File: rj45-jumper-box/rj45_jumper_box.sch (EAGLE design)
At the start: 4 parts, among them X1 SS-7188S-A-NF, X2 SS-7188S-A-NF

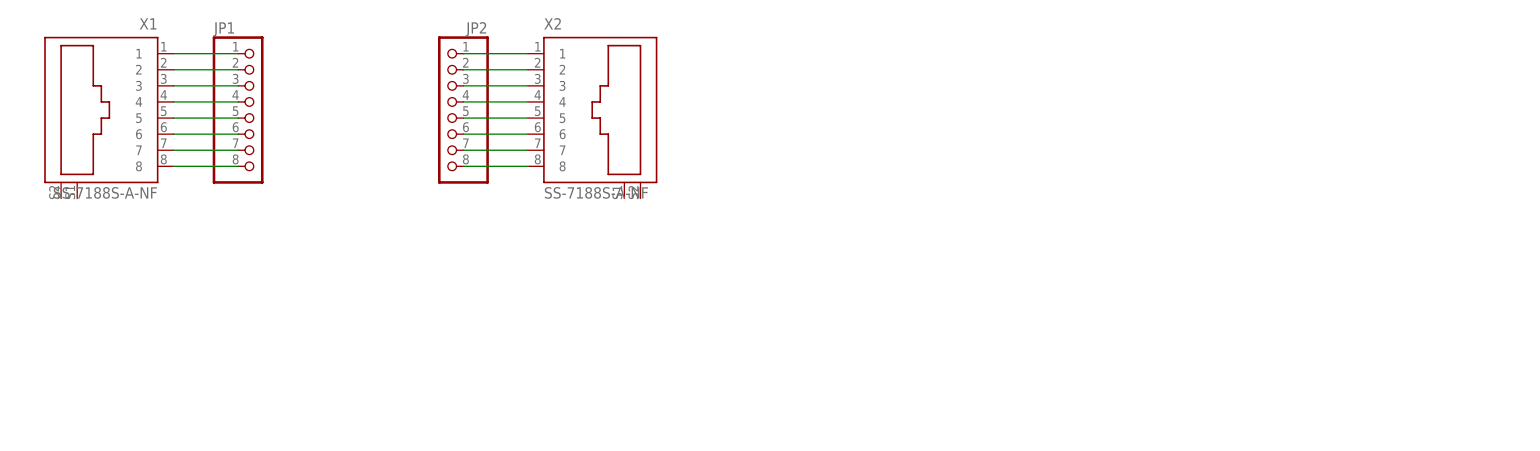
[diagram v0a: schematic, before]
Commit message: rj45_jumper_box: Use different RJ45 jack; both on top layer
The original design (one RJ45 on top, one on bottom) was easy to route
but was difficult to handle. Let's swap both connectors to top, and use
a low-cost Chinese RJ45.
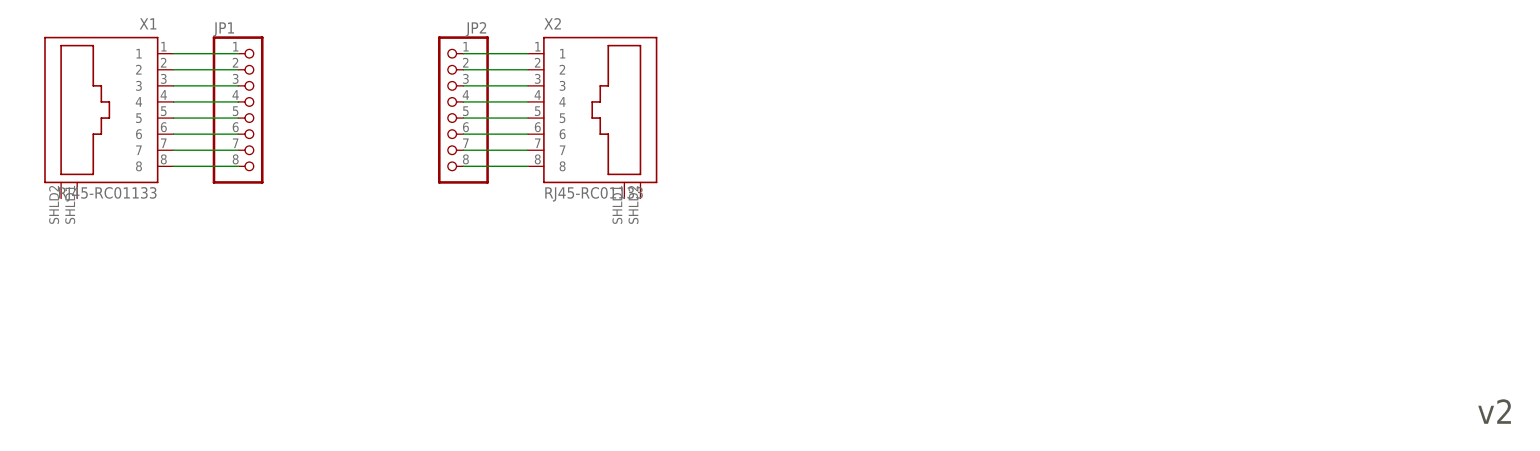
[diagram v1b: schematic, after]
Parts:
- X1, X2: value SS-7188S-A-NF -> RJ45-RC01133; device stewart-rj45:SS-7188S-A-NF -> stewart-rj45:RJ45-RC01133
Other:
- moved on the sheet: X1, X2
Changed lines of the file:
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@@
 <schematic xreflabel="%F%N/%S.%C%R" xrefpart="/%S.%C%R">
 <attributes>
+<attribute name="REVISION" value="v2"/>
 </attributes>
 <variantdefs>
@@
 </classes>
 <parts>
-<part name="X1" library="stewart-rj45" deviceset="SS-7188S-A-NF" device=""/>
-<part name="X2" library="stewart-rj45" deviceset="SS-7188S-A-NF" device=""/>
+<part name="X1" library="stewart-rj45" deviceset="RJ45" device="-RC01133"/>
+<part name="X2" library="stewart-rj45" deviceset="RJ45" device="-RC01133"/>
 <part name="FRAME1" library="frames" deviceset="DINA4_L" device=""/>
 <part name="JP1" library="pinhead" deviceset="PINHD-1X8" device=""/>
@@
 <sheet>
 <plain>
+<text x="256.54" y="7.62" size="3.81" layer="97" ratio="11">&gt;REVISION</text>
 </plain>
 <instances>

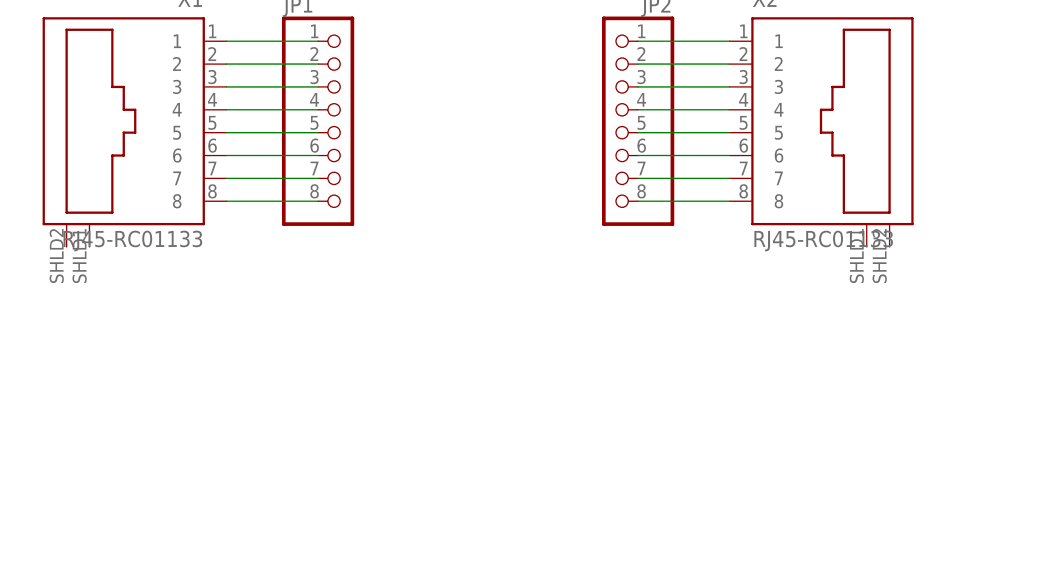
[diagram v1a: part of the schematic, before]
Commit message: rj45_jumper_box: Connect shield of two connectors
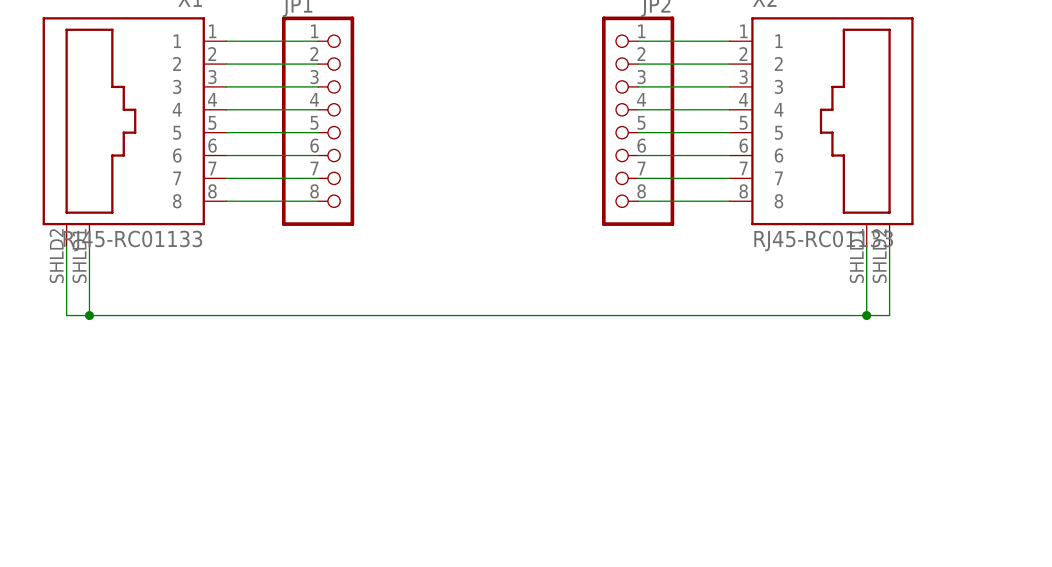
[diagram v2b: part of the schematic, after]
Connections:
- new net N$1: X1.S1, X1.S2, X2.S1, X2.S2
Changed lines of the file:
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@@
+</segment>
+</net>
+<net name="N$1" class="0">
+<segment>
+<pinref part="X1" gate="G$1" pin="S2"/>
+<wire x1="33.02" y1="43.18" x2="33.02" y2="35.56" width="0.1524" layer="91"/>
+<pinref part="X2" gate="G$1" pin="S2"/>
+<wire x1="33.02" y1="35.56" x2="35.56" y2="35.56" width="0.1524" layer="91"/>
+<wire x1="35.56" y1="35.56" x2="121.92" y2="35.56" width="0.1524" layer="91"/>
+<wire x1="121.92" y1="35.56" x2="124.46" y2="35.56" width="0.1524" layer="91"/>
+<wire x1="124.46" y1="35.56" x2="124.46" y2="43.18" width="0.1524" layer="91"/>
+<pinref part="X2" gate="G$1" pin="S1"/>
+<wire x1="121.92" y1="43.18" x2="121.92" y2="35.56" width="0.1524" layer="91"/>
+<pinref part="X1" gate="G$1" pin="S1"/>
+<wire x1="35.56" y1="43.18" x2="35.56" y2="35.56" width="0.1524" layer="91"/>
+<junction x="35.56" y="35.56"/>
+<junction x="121.92" y="35.56"/>
 </segment>
 </net>

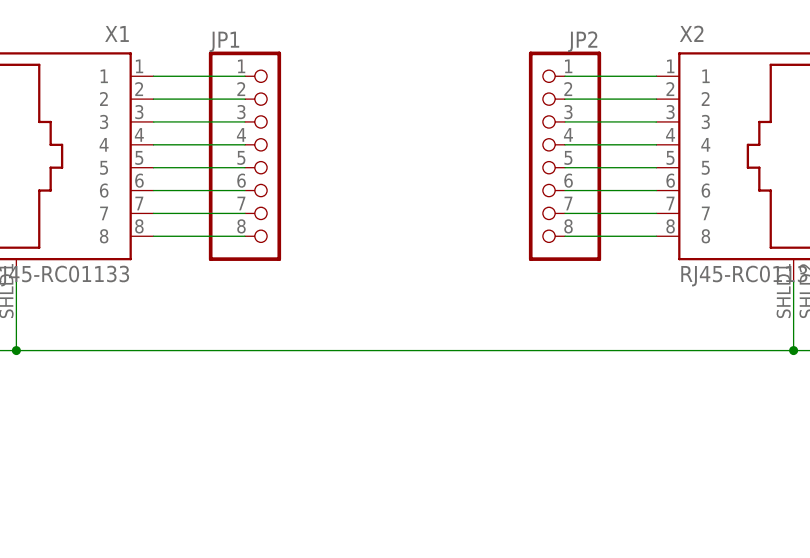
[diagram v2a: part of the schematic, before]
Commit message: rj45_jumper_box: Add OSWH + sysmocom logo; final v2 as ordered
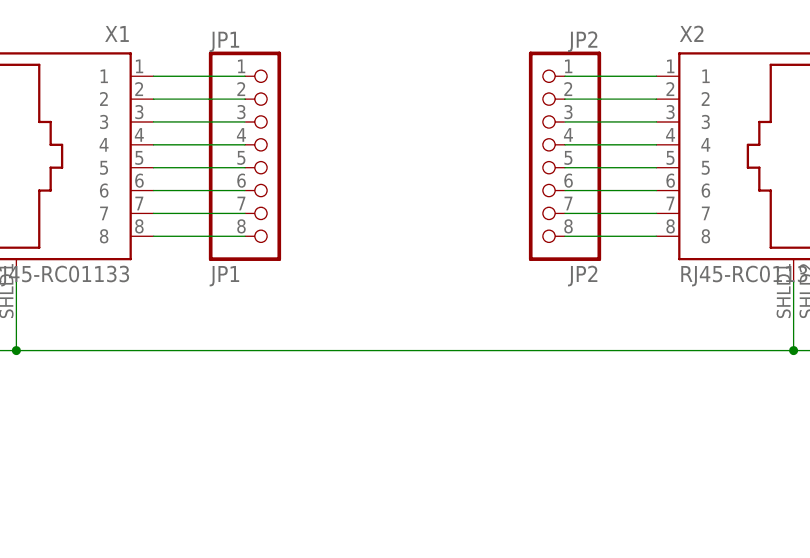
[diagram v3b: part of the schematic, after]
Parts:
- JP1: value (none) -> JP1
- JP2: value (none) -> JP2
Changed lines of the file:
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@@
 <part name="X2" library="stewart-rj45" deviceset="RJ45" device="-RC01133"/>
 <part name="FRAME1" library="frames" deviceset="DINA4_L" device=""/>
-<part name="JP1" library="pinhead" deviceset="PINHD-1X8" device=""/>
-<part name="JP2" library="pinhead" deviceset="PINHD-1X8" device=""/>
+<part name="JP1" library="pinhead" deviceset="PINHD-1X8" device="" value="JP1"/>
+<part name="JP2" library="pinhead" deviceset="PINHD-1X8" device="" value="JP2"/>
 </parts>
 <sheets>
